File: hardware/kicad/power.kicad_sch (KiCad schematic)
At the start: 22 parts, among them Q2 PMV32UP, Q7 DMG1012UW, U10 TPS7A0328DBVR, U12 TPS7A0333DBVR, U3 RT9080-33GJ5, U8 SY8089A1AAC

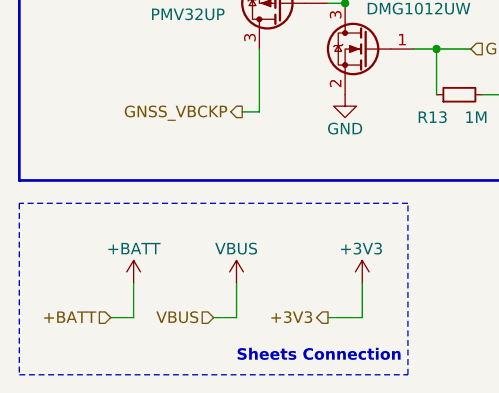
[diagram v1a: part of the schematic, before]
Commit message: GNSS and Antenna Update
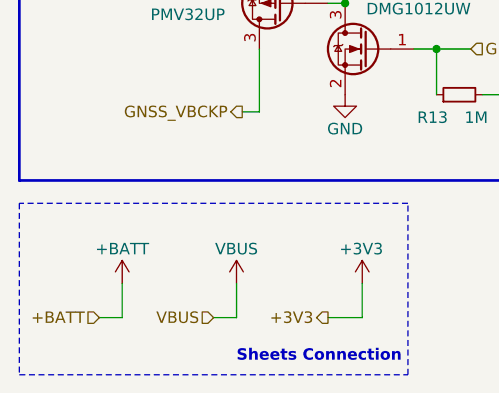
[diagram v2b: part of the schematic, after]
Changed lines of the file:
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@@
 	(wire
 		(pts
-			(xy 54.61 138.43) (xy 54.61 142.24)
+			(xy 53.34 138.43) (xy 53.34 142.24)
 		)
 		(stroke
@@
 	(wire
 		(pts
-			(xy 54.61 142.24) (xy 52.07 142.24)
+			(xy 53.34 142.24) (xy 50.8 142.24)
 		)
 		(stroke
@@
 	(hierarchical_label "+BATT"
 		(shape input)
-		(at 52.07 142.24 180)
+		(at 50.8 142.24 180)
 		(fields_autoplaced yes)
 		(effects
@@
 	(symbol
 		(lib_id "power:+BATT")
-		(at 54.61 138.43 0)
+		(at 53.34 138.43 0)
 		(unit 1)
 		(exclude_from_sim no)
@@
 		(dnp no)
 		(property "Reference" "#PWR0109"
-			(at 54.61 142.24 0)
+			(at 53.34 142.24 0)
 			(effects
 				(font
@@
 		)
 		(property "Value" "+BATT"
-			(at 54.61 134.62 0)
+			(at 53.34 134.62 0)
 			(effects
 				(font
@@
 		)
 		(property "Footprint" ""
-			(at 54.61 138.43 0)
+			(at 53.34 138.43 0)
 			(effects
 				(font
@@
 		)
 		(property "Datasheet" ""
-			(at 54.61 138.43 0)
+			(at 53.34 138.43 0)
 			(effects
 				(font
@@
 		)
 		(property "Description" ""
-			(at 54.61 138.43 0)
+			(at 53.34 138.43 0)
 			(effects
 				(font

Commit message: Update for PCB Layout
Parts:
- removed C24, C26: 1u, Capacitor_SMD:C_0603_1608Metric, symbol Device:C_Small
- removed U10: TPS7A0328DBVR, Package_TO_SOT_SMD:SOT-23-5, symbol Regulator_Linear:TPS7A0508PDBV
- renumbered C46 to C22, C56 to C23, C22 to C24, C55 to C25, C5 to C26, C20 to C27, C44 to C28, C45 to C29, L7 to L1, Q2 to Q5, Q7 to Q6, R43 to R24, R44 to R25, R12 to R26, R13 to R27, U8 to U4, U3 to U5, U12 to U6
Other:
- note removed: "GNSS 2V8 IO Power"

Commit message: update
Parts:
- added TP23, TP26, TP27, TP29, TP30: ~, TestPoint:TestPoint_Pad_D1.0mm, symbol Connector:TestPoint
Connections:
- net CELL_BATT: now also TP30.1
- net CELL_EN: now also TP29.1
- net GNSS_3V3: now also TP27.1
- net GNSS_EN: now also TP23.1
- net GNSS_VBCKP_EN: now also TP26.1
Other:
- moved on the sheet: C21, C22, C23, C24, C25, C26, C27, C28, C29, L1, Q5, Q6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

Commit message: Update Production File
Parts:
- renumbered C21 to C23, C22 to C24, C23 to C25, C24 to C26, C25 to C27, C26 to C28, C27 to C29, C28 to C30, C29 to C31, Q5 to Q1, Q6 to Q2, R24 to R16, R25 to R17, R26 to R18, R27 to R19, TP30 to TP27, TP29 to TP28, TP27 to TP29, TP23 to TP30, TP26 to TP31, U4 to U5, U5 to U6, U6 to U7
